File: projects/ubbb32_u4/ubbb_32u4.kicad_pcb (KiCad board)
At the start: 2 copper layers, 39.6 x 20.3 mm, 25 parts, among them CON1 USB-MINI-B, P2 CONN_5, P3 CONN_5, P4 CONN_5, P5 CONN_5, P6 CONN_5, P7 CONN_5, SW1 SW_PUSH_SMALL, SW2 SW_PUSH_SMALL, U1 ATMEGA32U4-A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

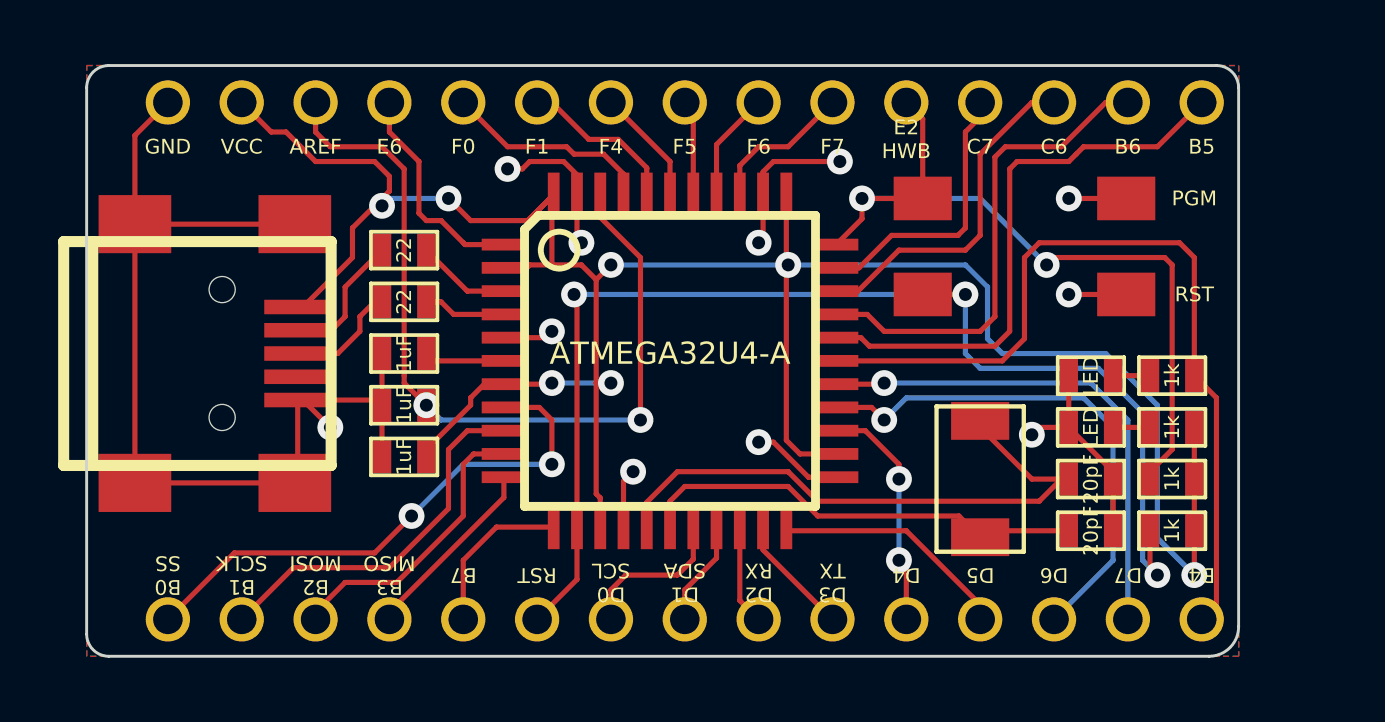
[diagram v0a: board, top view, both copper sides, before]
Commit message: Re-added ISP header on ubbb_32u4
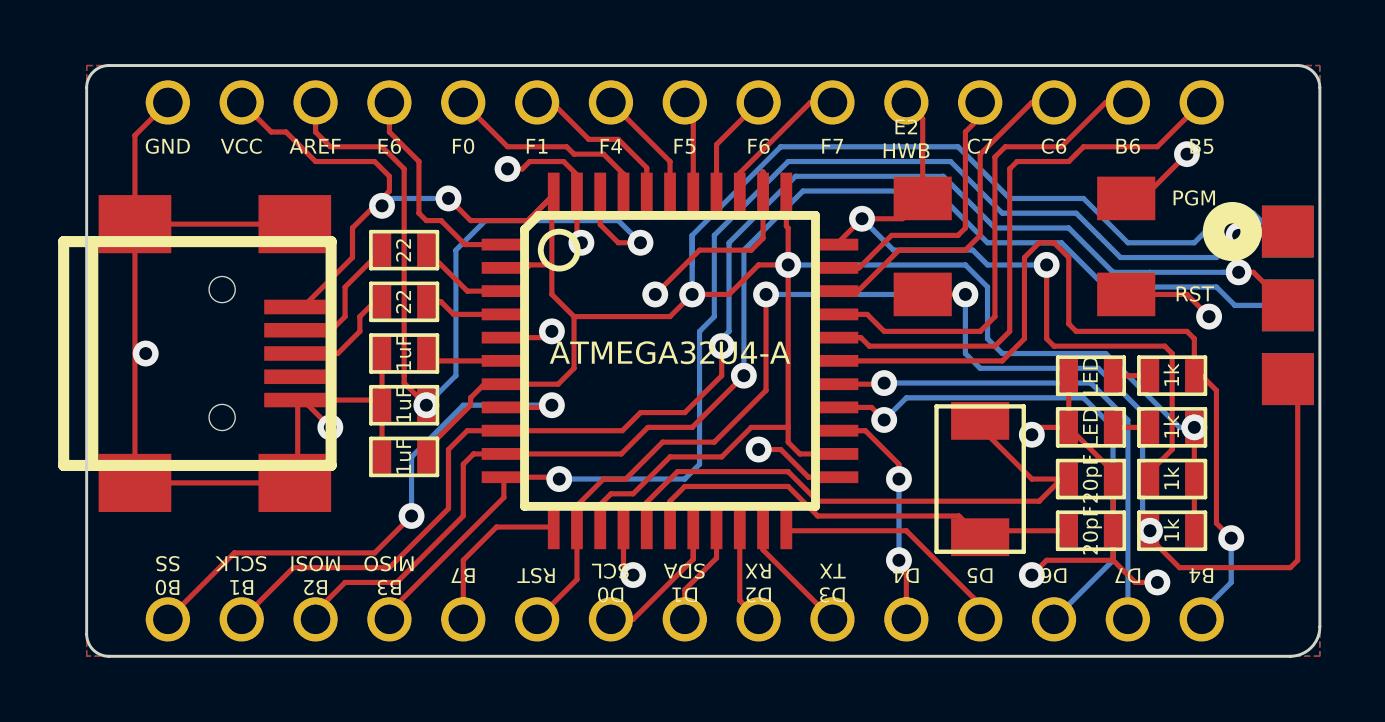
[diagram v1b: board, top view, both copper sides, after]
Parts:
- added P1: ISP, ISP_EDGE, F.Cu at (69.0, 40.0)
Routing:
- net /B3: track 6.52 -> 44.1 mm, vias 0 -> 2
- net /B1: track 12.9 -> 47.9 mm, vias 0 -> 2
- net /B2: track 10.0 -> 44.9 mm, vias 0 -> 1
- net +5V: track 87.3 -> 109.9 mm, vias 7 -> 5
- net GND: track 64.4 -> 74.5 mm, vias 11 -> 13
- net /RESET: track 43.1 -> 49.6 mm
- net /E2: track 27.1 -> 25.9 mm
- net /D0: track 5.39 -> 5.90 mm
- net /B4: track 28.8 -> 29.1 mm, vias 0 -> 1
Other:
- board size 39.6 x 20.3 mm -> 42.4 x 20.3 mm

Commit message: Change status light to be RGB LED
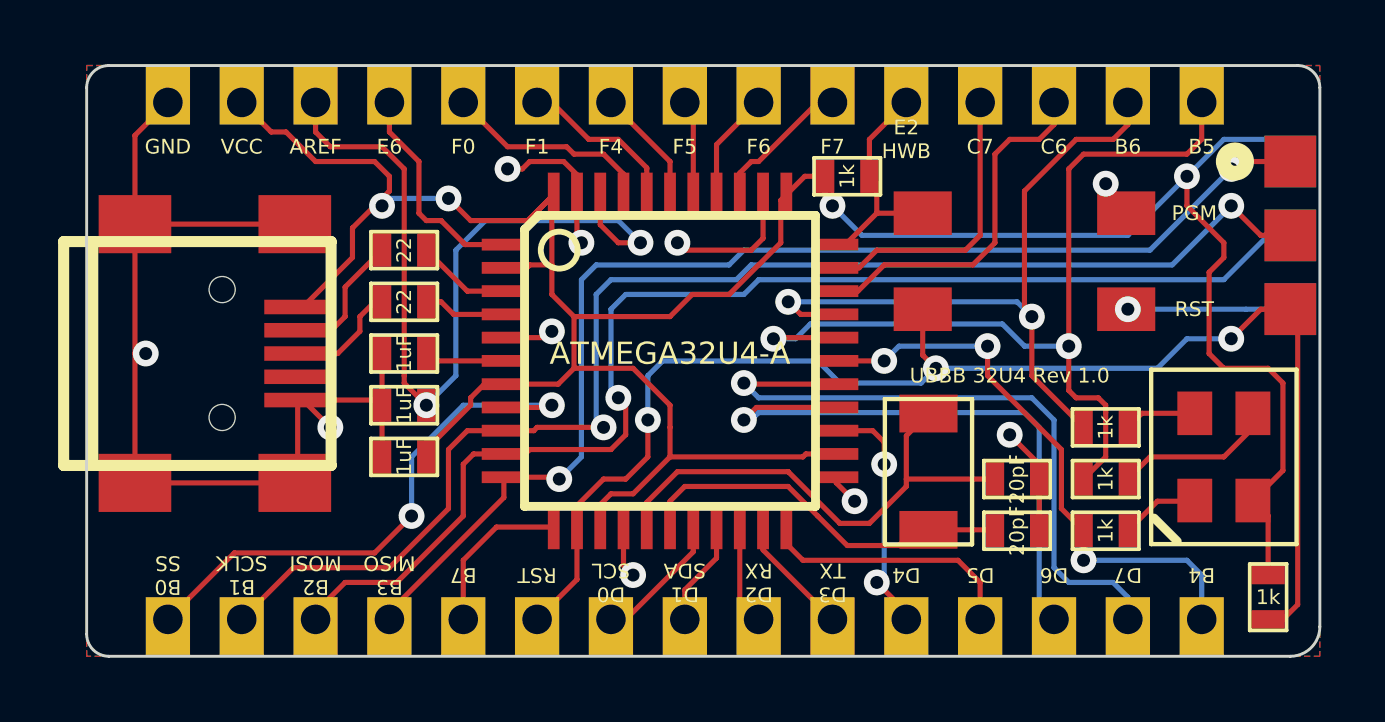
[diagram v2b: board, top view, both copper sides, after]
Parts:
- removed D1: LED, SM0603_VALUE
- removed R1: 1k, SM0603_VALUE
- added R7: 1k, SM0603_VALUE, F.Cu at (60.2, 46.0)
- added R8: 1k, SM0603_VALUE, F.Cu at (60.2, 44.2)
- added WJ10: VAL**, WJ10, B.Cu at (46.7, 41.9)
- D2: value LED -> RGB_LED_COMMON_ANODE; footprint SM0603_VALUE -> LED_RGB_4-PLCC
- moved R6 15.3 mm to (51.3, 35.6), turned to 180 degrees
- moved R5 5.80 mm to (60.2, 47.8)
- moved D2 5.36 mm to (64.3, 45.2), turned to 90 degrees
- moved R4 4.02 mm to (65.8, 50.0), turned to 270 degrees
- moved C1 2.54 mm to (57.1, 47.8)
- moved C2 2.54 mm to (57.1, 46.0)
- moved P1 2.41 mm to (69.1, 37.6)
- moved X1 1.80 mm to (54.1, 45.7)
- moved VAL 1.48 mm to (58.4, 41.1), turned to 0 degrees
- moved SW1 0.51 mm to (57.4, 40.1)
- moved SW2 0.51 mm to (57.4, 36.8)
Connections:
- D2 pad 1: N-0000038 -> N-0000012
- D2 pad 2: GND -> +5V
- R5 pad 1: /B4 -> N-0000012
- R5 pad 2: N-0000038 -> /B4
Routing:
- net /E2: track 25.9 -> 7.87 mm, vias 2 -> 0
- net GND: track 74.5 -> 61.2 mm, vias 13 -> 11
- net +5V: track 109.9 -> 97.5 mm, vias 5 -> 4
- net /B5: track 19.4 -> 31.1 mm, vias 0 -> 2
- net /B4: track 29.1 -> 19.9 mm, vias 1 -> 3
- net /B6: track 16.8 -> 24.7 mm, vias 0 -> 2
- net /D7: track 17.4 -> 23.2 mm
- net N-0000011: track 0.00 -> 5.53 mm
- net N-0000035: track 20.5 -> 17.4 mm
- net /D6: track 17.9 -> 20.6 mm
- net N-0000012: track 0.00 -> 2.73 mm
- net N-0000010: track 0.00 -> 2.50 mm
- net /B3: track 44.1 -> 41.7 mm
- net N-0000041: track 15.6 -> 13.4 mm
- net /RESET: track 49.6 -> 47.8 mm
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
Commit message: Added mounting holes to 32u4 dev board
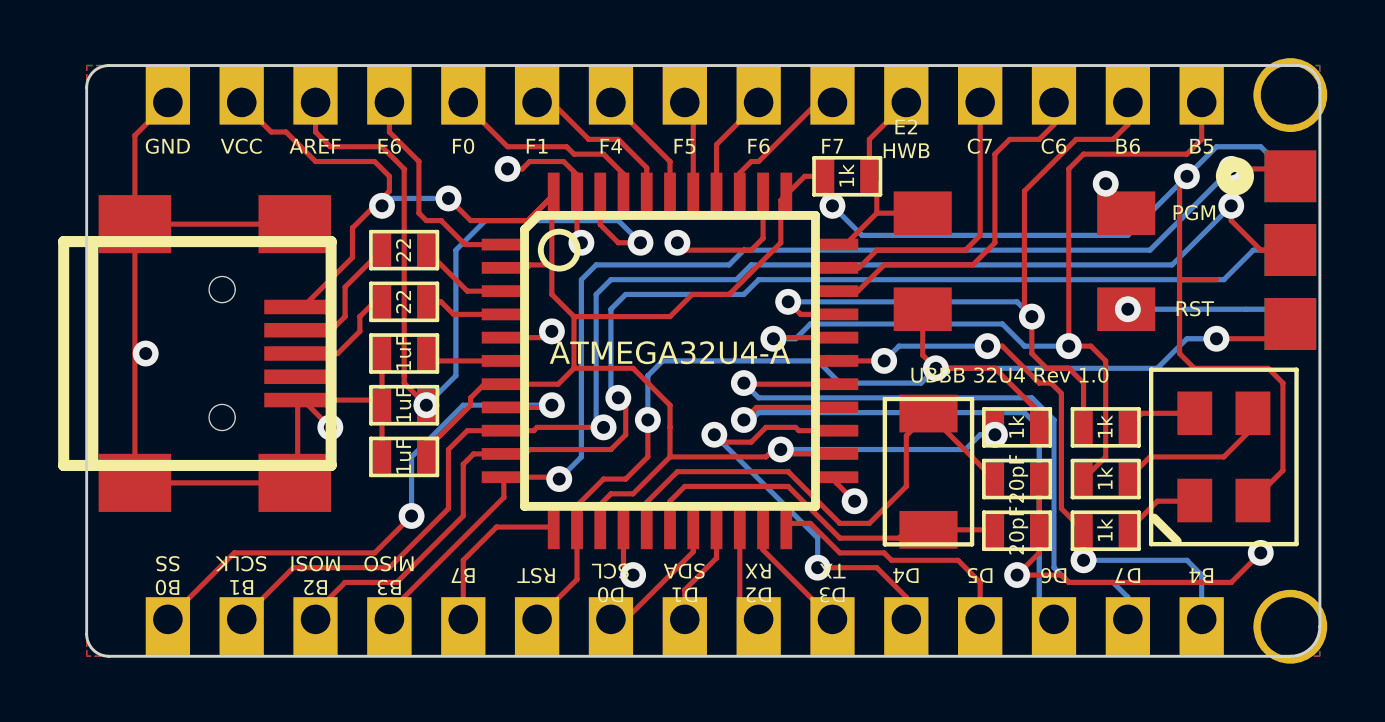
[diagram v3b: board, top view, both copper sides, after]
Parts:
- added 1PIN: P***, 1pin, F.Cu at (66.5, 51.1)
- added 1PIN: P***, 1pin, F.Cu at (66.5, 32.8)
- moved R4 10.4 mm to (57.1, 44.2), turned to 0 degrees
- moved P1 0.51 mm to (69.1, 38.1)
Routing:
- net GND: track 61.2 -> 70.2 mm, vias 11 -> 12
- net /RESET: track 47.8 -> 40.8 mm
- net +5V: track 97.5 -> 104.3 mm, vias 4 -> 6
- net /D4: track 8.44 -> 14.8 mm
- net /B4: track 19.9 -> 20.5 mm
- net /B1: track 46.6 -> 47.1 mm

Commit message: Adding USB pads for soldering on the bottom
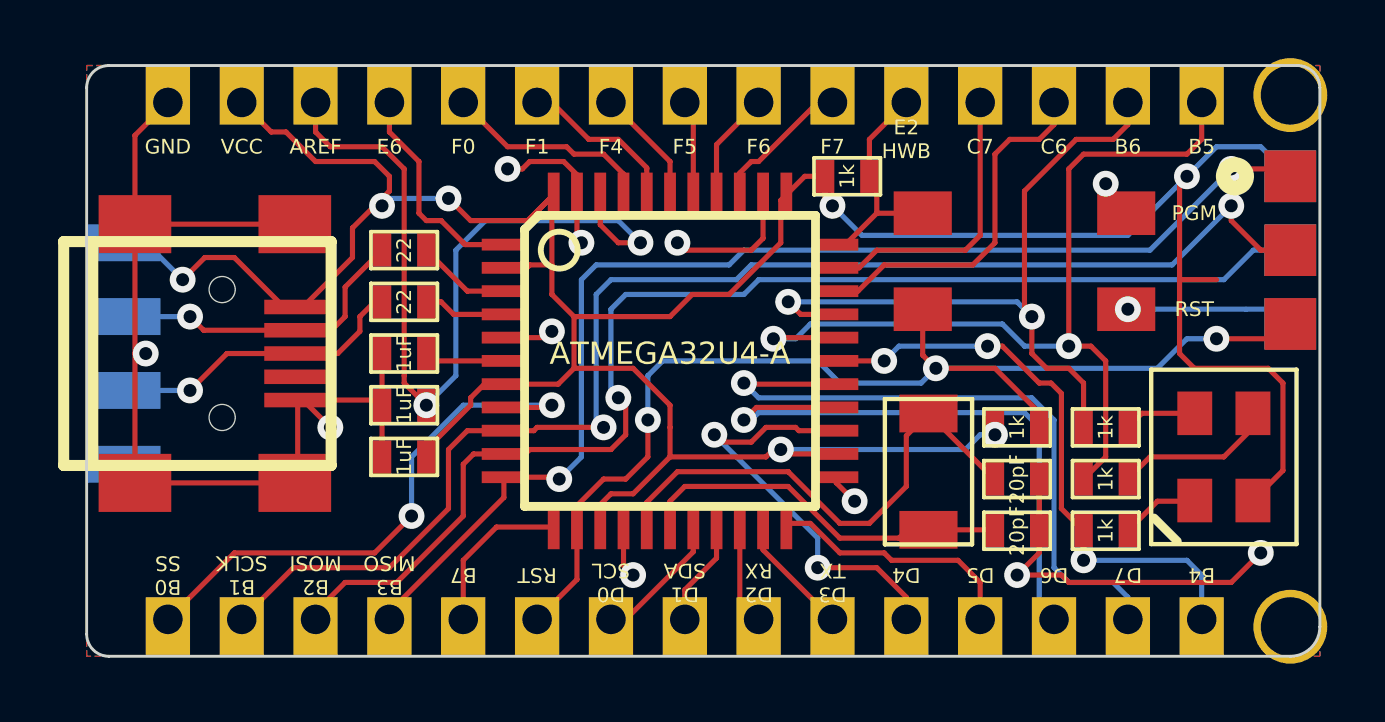
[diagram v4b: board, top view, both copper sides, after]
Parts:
- added PIN_ARRAY_4X1: Val**, PIN_ARRAY_4x1, B.Cu at (26.4, 41.7)
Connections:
- net N-0000017 renamed /D+
- net N-0000018 renamed /D-
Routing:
- net +5V: track 104.3 -> 111.9 mm, vias 6 -> 7
- net /D+: track 3.93 -> 10.5 mm, vias 0 -> 1
- net /D-: track 4.64 -> 10.8 mm, vias 0 -> 1
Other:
- board text added: "D+"
- board text added: "D-"
- board text added: "VUSB (+5V)"

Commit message: Moved /HWB pullup to a better location...
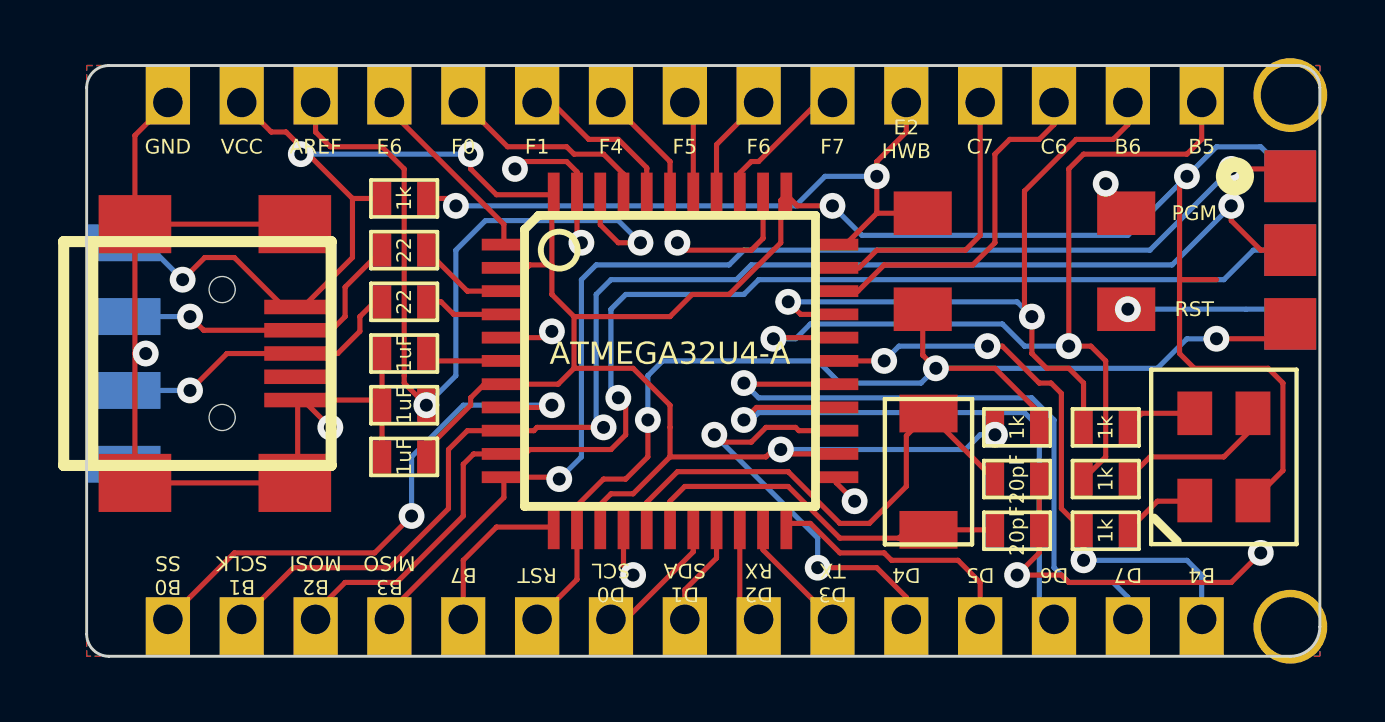
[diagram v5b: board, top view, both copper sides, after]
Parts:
- moved R6 15.3 mm to (36.1, 36.3)
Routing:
- net /E2: track 7.87 -> 23.7 mm, vias 0 -> 2
- net /E6: track 7.60 -> 6.77 mm

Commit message: A bit more cleanup on u4 board
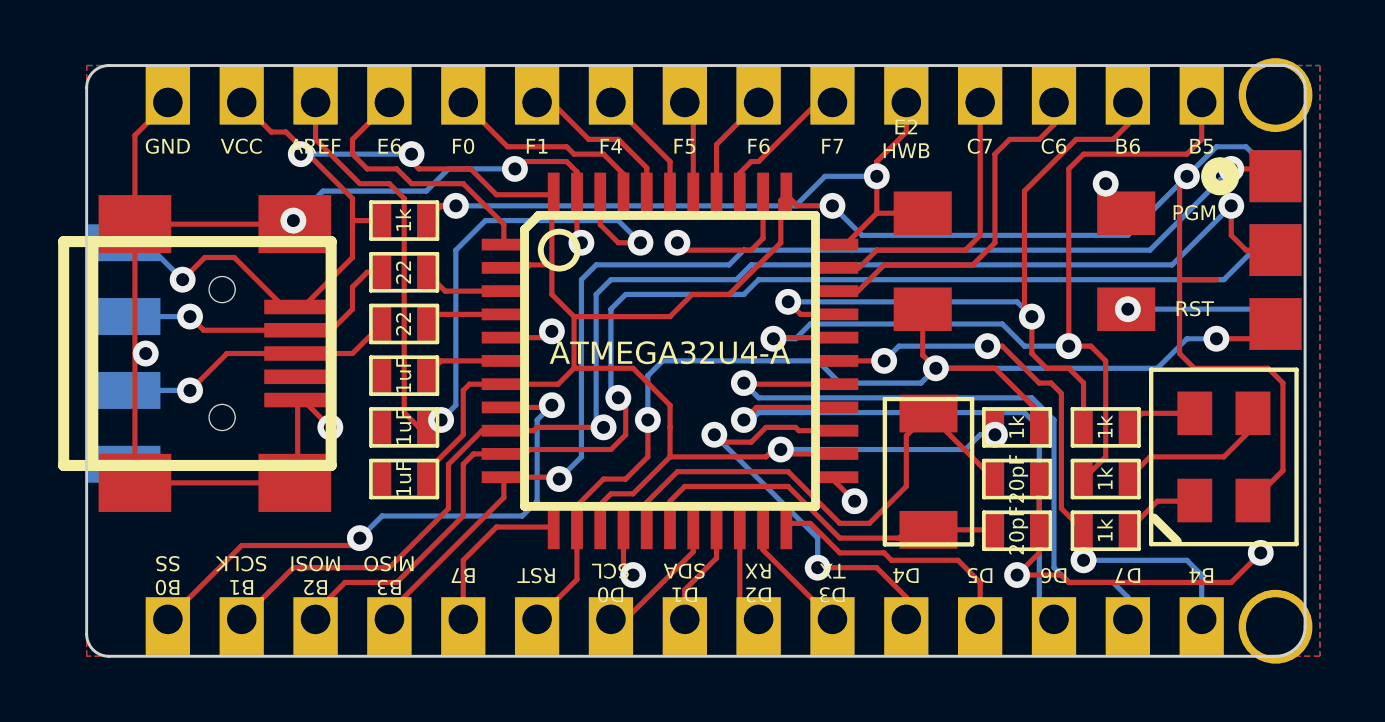
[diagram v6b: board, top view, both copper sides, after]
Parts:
- removed the VAL at (58.4, 41.1)
- added DIGITALCAVE_URL: VAL**, DIGITALCAVE_URL, B.Cu at (53.3, 42.2)
- added VAL: REF, DIGITALCAVE_LOGO, B.Cu at (61.5, 40.6)
- added VAL: DIGITALCAVE_AUTHOR, DIGITALCAVE_AUTHOR, B.Cu at (55.1, 40.4)
- moved WJ10 3.84 mm to (42.9, 41.4)
- moved C3 0.76 mm to (36.1, 44.2)
- moved C4 0.76 mm to (36.1, 42.4)
- moved R2 0.76 mm to (36.1, 40.6)
- moved R3 0.76 mm to (36.1, 38.9)
- moved R6 0.76 mm to (36.1, 37.1)
- moved C5 0.76 mm to (36.1, 46.0)
- moved 1PIN 0.51 mm to (66.0, 51.1)
- moved 1PIN 0.51 mm to (66.0, 32.8)
- moved P1 0.51 mm to (68.6, 38.1)
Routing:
- net /E6: track 6.77 -> 9.72 mm
- net GND: track 69.8 -> 71.2 mm, vias 12 -> 13
- net /AREF: track 28.5 -> 29.9 mm
- net /D+: track 10.5 -> 9.84 mm
- net /RESET: track 40.8 -> 40.3 mm
- net /B3: track 41.7 -> 41.2 mm
- net /B2: track 43.2 -> 42.7 mm
- net /B1: track 47.1 -> 46.6 mm
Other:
- board size 42.4 x 20.3 mm -> 41.9 x 20.3 mm

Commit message: More WIP on u4
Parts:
- removed C1, C2: 20pF, SM0603_VALUE
- X1: value CRYSTAL -> RESONATOR; footprint CRYSTAL_SMD_5x3.2 -> RESONATOR_SMD-3
- moved R6 19.4 mm to (54.1, 44.2), turned to 0 degrees
- moved X1 1.28 mm to (54.0, 47.0), turned to 90 degrees
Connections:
- U1 pad 16: N-0000035 -> N-0000016
- U1 pad 17: N-0000041 (its old number) -> N-0000017
- X1 pad 1: N-0000035 -> N-0000017
- X1 pad 2: N-0000041 (its old number) -> GND
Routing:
- net N-0000035: track 17.5 -> 0.00 mm
- net N-0000017: track 0.00 -> 13.2 mm
- net N-0000041 (its old number): track 13.1 -> 0.00 mm
- net N-0000016: track 0.00 -> 12.8 mm
- net (no net): track 0.00 -> 12.5 mm, vias 0 -> 2
- net GND: track 71.2 -> 58.8 mm, vias 13 -> 12
